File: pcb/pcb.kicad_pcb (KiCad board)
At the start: 2 copper layers, 34 parts, among them J1 Conn_01x20_Socket, J10 Conn_01x01_Socket, J11 Conn_01x01_Socket, J12 Conn_01x01_Socket, J13 Conn_01x01_Socket, J14 Conn_01x01_Socket, J15 Conn_01x01_Socket, J16 Conn_01x01_Socket, J17 Conn_01x01_Socket, J18 Conn_01x01_Socket, J19 Conn_01x01_Socket, J2 Conn_01x20_Socket, J20 Conn_01x01_Socket, J21 Conn_01x01_Socket, J22 Conn_01x01_Socket, J23 Conn_01x01_Socket, J24 Conn_01x01_Socket, J25 Conn_01x01_Socket, J26 Conn_01x01_Socket, J27 Conn_01x01_Socket, J28 Conn_01x01_Socket, J29 Conn_01x01_Socket, J3 Conn_01x01_Socket, J30 Conn_01x01_Socket, J31 Conn_01x01_Socket, J32 Conn_01x01_Socket, J33 Conn_01x01_Socket, J34 Conn_01x01_Socket, J4 Conn_01x01_Socket, J5 Conn_01x01_Socket, J6 Conn_01x01_Socket, J7 Conn_01x01_Socket, J8 Conn_01x01_Socket, J9 Conn_01x01_Socket

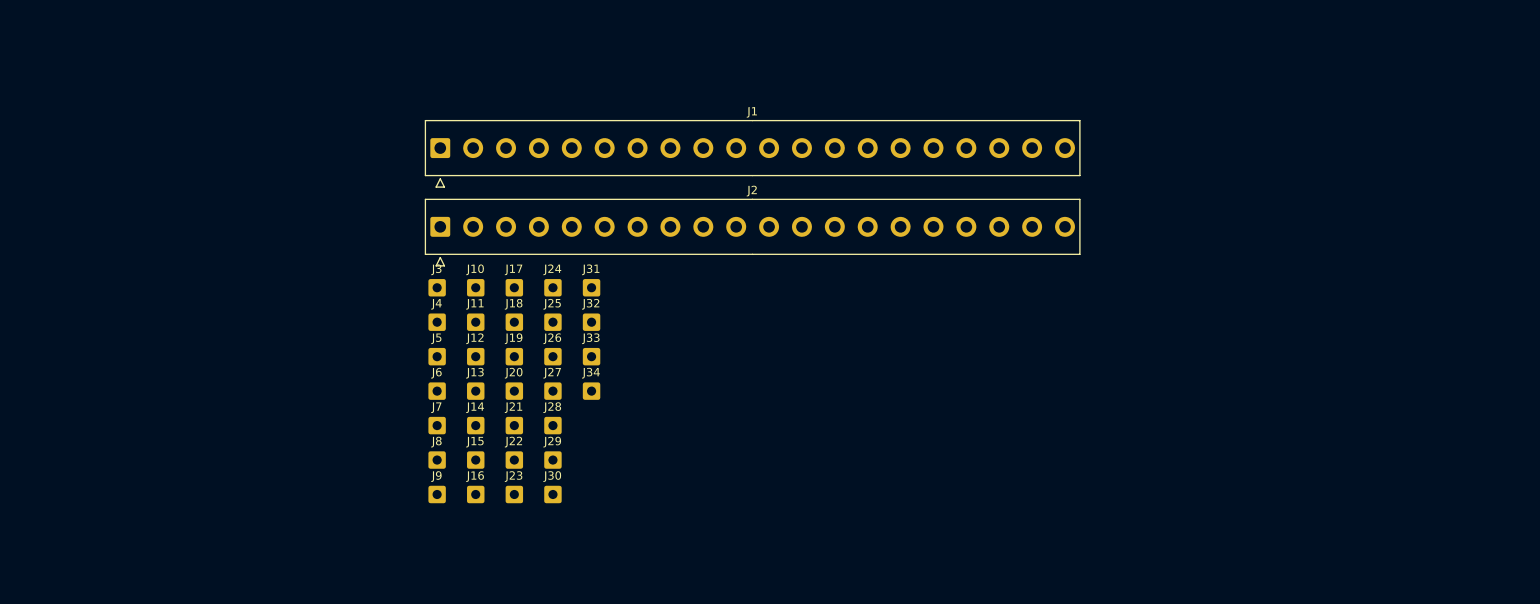
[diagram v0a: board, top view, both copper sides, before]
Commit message: I accidentally set up the project using the wrong folder, so I hope this fixes it. All these new files are the real project. Anyway, fixed issues with ADC breaking the MIDI connection. Small crash when doing multiple inputs at the same time. Next is to finally finish the PCB.
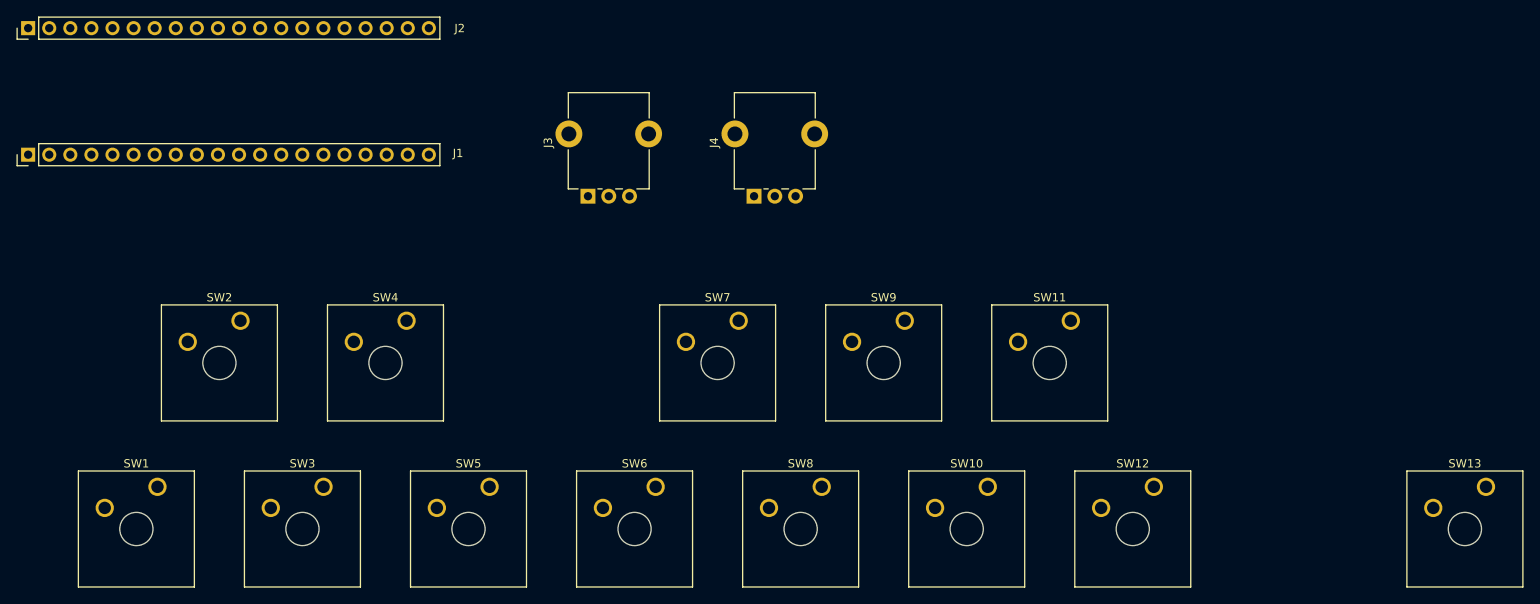
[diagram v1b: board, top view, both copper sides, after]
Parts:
- removed J10, J11, J12, J13, J14, J15, J16, J17, J18, J19, J20, J21, J22, J23, J24, J25, J26, J27, J28, J29, J30, J31, J32, J33, J34, J5, J6, J7, J8, J9: Conn_01x01_Socket, Connector_Wire:SolderWire-0.5sqmm_1x01_D0.9mm_OD2.1mm
- added SW1: SW_Push, Button_Switch_Keyboard:SW_Cherry_MX_1.00u_Plate, F.Cu at (82.7, 118.3)
- added SW10: SW_Push, Button_Switch_Keyboard:SW_Cherry_MX_1.00u_Plate, F.Cu at (182.7, 118.3)
- added SW11: SW_Push, Button_Switch_Keyboard:SW_Cherry_MX_1.00u_Plate, F.Cu at (192.7, 98.3)
- added SW12: SW_Push, Button_Switch_Keyboard:SW_Cherry_MX_1.00u_Plate, F.Cu at (202.7, 118.3)
- added SW13: SW_Push, Button_Switch_Keyboard:SW_Cherry_MX_1.00u_Plate, F.Cu at (242.7, 118.3)
- added SW2: SW_Push, Button_Switch_Keyboard:SW_Cherry_MX_1.00u_Plate, F.Cu at (92.7, 98.3)
- added SW3: SW_Push, Button_Switch_Keyboard:SW_Cherry_MX_1.00u_Plate, F.Cu at (102.7, 118.3)
- added SW4: SW_Push, Button_Switch_Keyboard:SW_Cherry_MX_1.00u_Plate, F.Cu at (112.7, 98.3)
- added SW5: SW_Push, Button_Switch_Keyboard:SW_Cherry_MX_1.00u_Plate, F.Cu at (122.7, 118.3)
- added SW6: SW_Push, Button_Switch_Keyboard:SW_Cherry_MX_1.00u_Plate, F.Cu at (142.7, 118.3)
- added SW7: SW_Push, Button_Switch_Keyboard:SW_Cherry_MX_1.00u_Plate, F.Cu at (152.7, 98.3)
- added SW8: SW_Push, Button_Switch_Keyboard:SW_Cherry_MX_1.00u_Plate, F.Cu at (162.7, 118.3)
- added SW9: SW_Push, Button_Switch_Keyboard:SW_Cherry_MX_1.00u_Plate, F.Cu at (172.7, 98.3)
- J1, J2: footprint Connector_TE-Connectivity:TE_2-826576-0_1x20_P3.96mm_Vertical -> Connector_PinHeader_2.54mm:PinHeader_1x20_P2.54mm_Vertical
- J3, J4: value Conn_01x01_Socket -> Conn_01x03_Socket; footprint Connector_Wire:SolderWire-0.5sqmm_1x01_D0.9mm_OD2.1mm -> Potentiometer_THT:Potentiometer_Alpha_RD901F-40-00D_Single_Vertical_CircularHoles
- moved J2 55.1 mm to (67.1, 63.1), turned to 90 degrees
- moved J1 49.6 mm to (67.1, 78.3), turned to 90 degrees
- moved J4 41.1 mm to (154.6, 83.3), turned to 90 degrees
- moved J3 21.3 mm to (134.6, 83.3), turned to 90 degrees
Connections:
- J2 pad 1: VB -> G
- J2 pad 10: A5 -> A6
- J2 pad 11: A6 -> A5
- J2 pad 12: A7 -> A4
- J2 pad 13: B0 -> A3
- J2 pad 14: B1 -> A2
- J2 pad 15: B10 -> A1
- J2 pad 16: B11 -> A0
- J2 pad 17: R -> C15
- J2 pad 18: 3.3 -> C14
- J2 pad 19: G -> C13
- J2 pad 2: C13 -> G
- J2 pad 20: G -> VB
- J2 pad 3: C14 -> 3.3
- J2 pad 4: C15 -> R
- J2 pad 5: A0 -> B11
- J2 pad 6: A1 -> B10
- J2 pad 7: A2 -> B1
- J2 pad 8: A3 -> B0
- J2 pad 9: A4 -> A7
- J3 pad 1: G -> 5V
- J4 pad 1: A2 -> 5V
